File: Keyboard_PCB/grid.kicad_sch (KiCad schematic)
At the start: 140 parts, among them SW1 ESC, SW10 9, SW11 0, SW12 -, SW13 =, SW14 <-, SW15 DEL, SW16 TAB, SW17 Q, SW18 W, SW19 E, SW2 1, SW20 R, SW21 T, SW22 Y, SW23 U, SW24 I, SW25 O, SW26 P, SW27 [, SW28 ], SW29 \, SW3 2, SW30 HOME, SW31 CAPS, SW32 A, SW33 S, SW34 D, SW35 F, SW36 G, SW37 H, SW38 J, SW39 K, SW4 3, SW40 L, SW41 ;, SW42 ', SW43 ENTER, SW44 PG_U, SW45 SHIFT, SW46 Z, SW47 X, SW48 C, SW49 V, SW5 4, SW50 B, SW51 N, SW52 M, SW53 ,, SW54 ., SW55 /, SW56 SHIFT, SW57 UP, SW58 PG_D, SW59 CTRL, SW6 5, SW60 CODE, SW61 ALT, SW62 SPACE, SW63 ALT, SW64 CODE, SW65 CTRL, SW66 LEFT, SW67 DOWN, SW68 RIGHT, SW69 EC11E15244G1, SW7 6, SW8 7, SW9 8

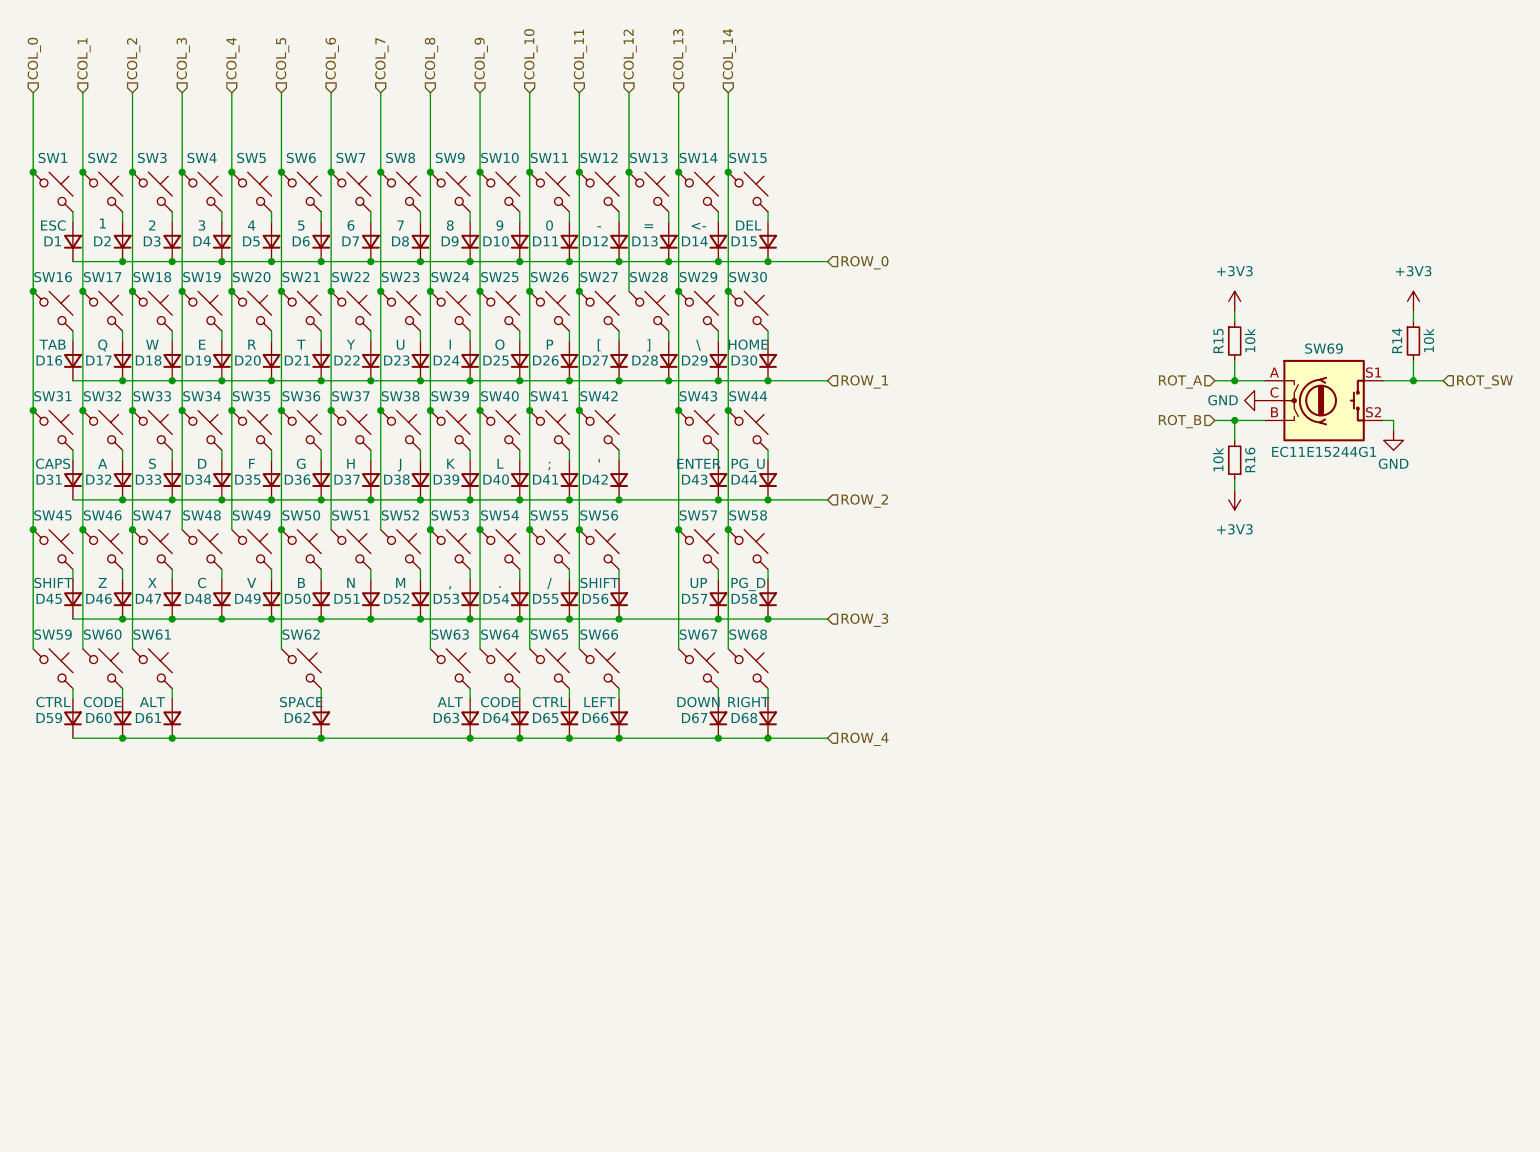
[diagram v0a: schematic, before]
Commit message: Fixed errors in BOM file
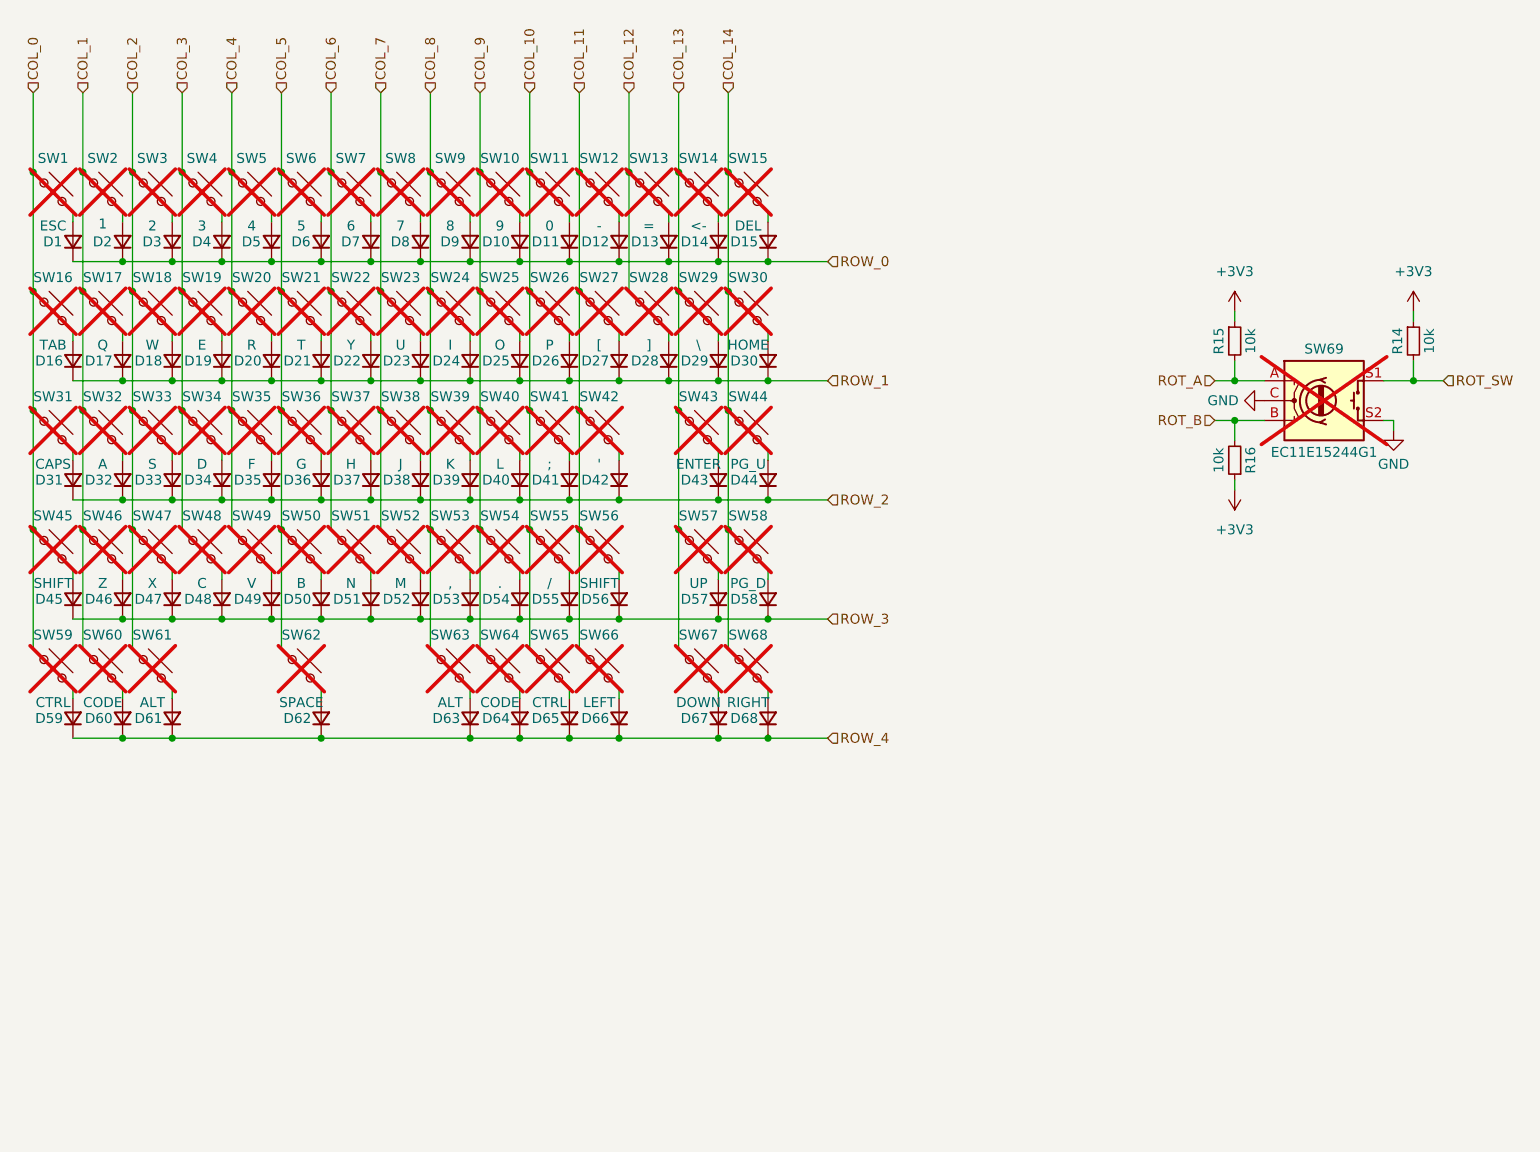
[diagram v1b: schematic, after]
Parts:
- SW1, SW10, SW11, SW12, SW13, SW14, SW15, SW16, SW17, SW18, SW19, SW2, SW20, SW21, SW22, SW23, SW24, SW25, SW26, SW27, SW28, SW29, SW3, SW30, SW31, SW32, SW33, SW34, SW35, SW36, SW37, SW38, SW39, SW4, SW40, SW41, SW42, SW43, SW44, SW45, SW46, SW47, SW48, SW49, SW5, SW50, SW51, SW52, SW53, SW54, SW55, SW56, SW57, SW58, SW59, SW6, SW60, SW61, SW62, SW63, SW64, SW65, SW66, SW67, SW68, SW69, SW7, SW8, SW9: now not fitted

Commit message: Found error in BOM
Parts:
- R14, R15, R16: LCSC C25879 -> C25744
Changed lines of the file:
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@@
 			)
 		)
-		(property "LCSC" "C25879"
+		(property "LCSC" "C25744"
 			(at 217.17 82.55 0)
 			(effects
@@
 			)
 		)
-		(property "LCSC" "C25879"
+		(property "LCSC" "C25744"
 			(at 240.03 82.55 0)
 			(effects
@@
 			)
 		)
-		(property "LCSC" "C25879"
+		(property "LCSC" "C25744"
 			(at 217.17 97.79 0)
 			(effects

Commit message: LCD-overhead test
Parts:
- added R14, R16, R6: 10k, Resistor_SMD:R_0402_1005Metric, symbol Device:R_Small
- added SW70: EC11E15244G1, Rotary_Encoder:RotaryEncoder_Alps_EC11E-Switch_Vertical_H20mm, symbol Device:RotaryEncoder_Switch
- renumbered R16 to R15, R15 to R4, R14 to R5
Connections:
- net +3V3: now also R14.1, R16.1, R6.1
- net GND: now also SW70.C, SW70.S2
- net ROT_A: now also R6.2, SW70.A
- net ROT_B: now also R16.2, SW70.B
- net ROT_SW: now also R14.2, SW70.S1
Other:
- moved on the sheet: R15, R4, R5, SW69

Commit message: USB placement
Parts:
- SW69: footprint Rotary_Encoder:RotaryEncoder_Alps_EC11E-Switch_Vertical_H20mm -> Marijn_KiCad:EC11E-Switch-No_MP
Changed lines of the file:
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@@
 			)
 		)
-		(property "Footprint" "Rotary_Encoder:RotaryEncoder_Alps_EC11E-Switch_Vertical_H20mm"
+		(property "Footprint" "Marijn_KiCad:EC11E-Switch-No_MP"
 			(at 81.28 162.306 0)
 			(effects

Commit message: Layout progress
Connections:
- net ROT_A renamed ROT0_A
- net ROT0_A: no longer R6.2, SW70.A
- net ROT_B renamed ROT0_B
- net ROT0_B: no longer R16.2, SW70.B
- net ROT_SW renamed ROT0_SW
- net ROT0_SW: no longer R14.2, SW70.S1
- new net ROT1_A: R6.2, SW70.A
- new net ROT1_B: R16.2, SW70.B
- new net ROT1_SW: R14.2, SW70.S1
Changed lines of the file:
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@@
 		)
 	)
-	(hierarchical_label "ROT_SW"
+	(hierarchical_label "ROT0_SW"
 		(shape input)
 		(at 100.33 163.83 0)
@@
 		)
 	)
-	(hierarchical_label "ROT_B"
+	(hierarchical_label "ROT0_B"
 		(shape input)
 		(at 71.12 168.91 180)
@@
 		)
 	)
-	(hierarchical_label "ROT_B"
+	(hierarchical_label "ROT1_B"
 		(shape input)
 		(at 124.46 168.91 180)
@@
 		)
 	)
-	(hierarchical_label "ROT_A"
+	(hierarchical_label "ROT0_A"
 		(shape input)
 		(at 71.12 163.83 180)
@@
 		)
 	)
-	(hierarchical_label "ROT_A"
+	(hierarchical_label "ROT1_A"
 		(shape input)
 		(at 124.46 163.83 180)
@@
 		)
 	)
-	(hierarchical_label "ROT_SW"
+	(hierarchical_label "ROT1_SW"
 		(shape input)
 		(at 153.67 163.83 0)

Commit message: Finished Layout V1
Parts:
- R14, R15, R16, R4, R5, R6: footprint Resistor_SMD:R_0402_1005Metric -> Resistor_SMD:R_0603_1608Metric
- SW1, SW10, SW11, SW12, SW13, SW14, SW15, SW16, SW17, SW18, SW19, SW2, SW20, SW21, SW22, SW23, SW24, SW25, SW26, SW27, SW28, SW29, SW3, SW30, SW31, SW32, SW33, SW34, SW35, SW36, SW37, SW38, SW39, SW4, SW40, SW41, SW42, SW43, SW44, SW45, SW46, SW47, SW48, SW49, SW5, SW50, SW51, SW52, SW53, SW54, SW55, SW56, SW57, SW58, SW59, SW6, SW60, SW61, SW62, SW63, SW64, SW65, SW66, SW67, SW68, SW69, SW7, SW70, SW8, SW9: now fitted

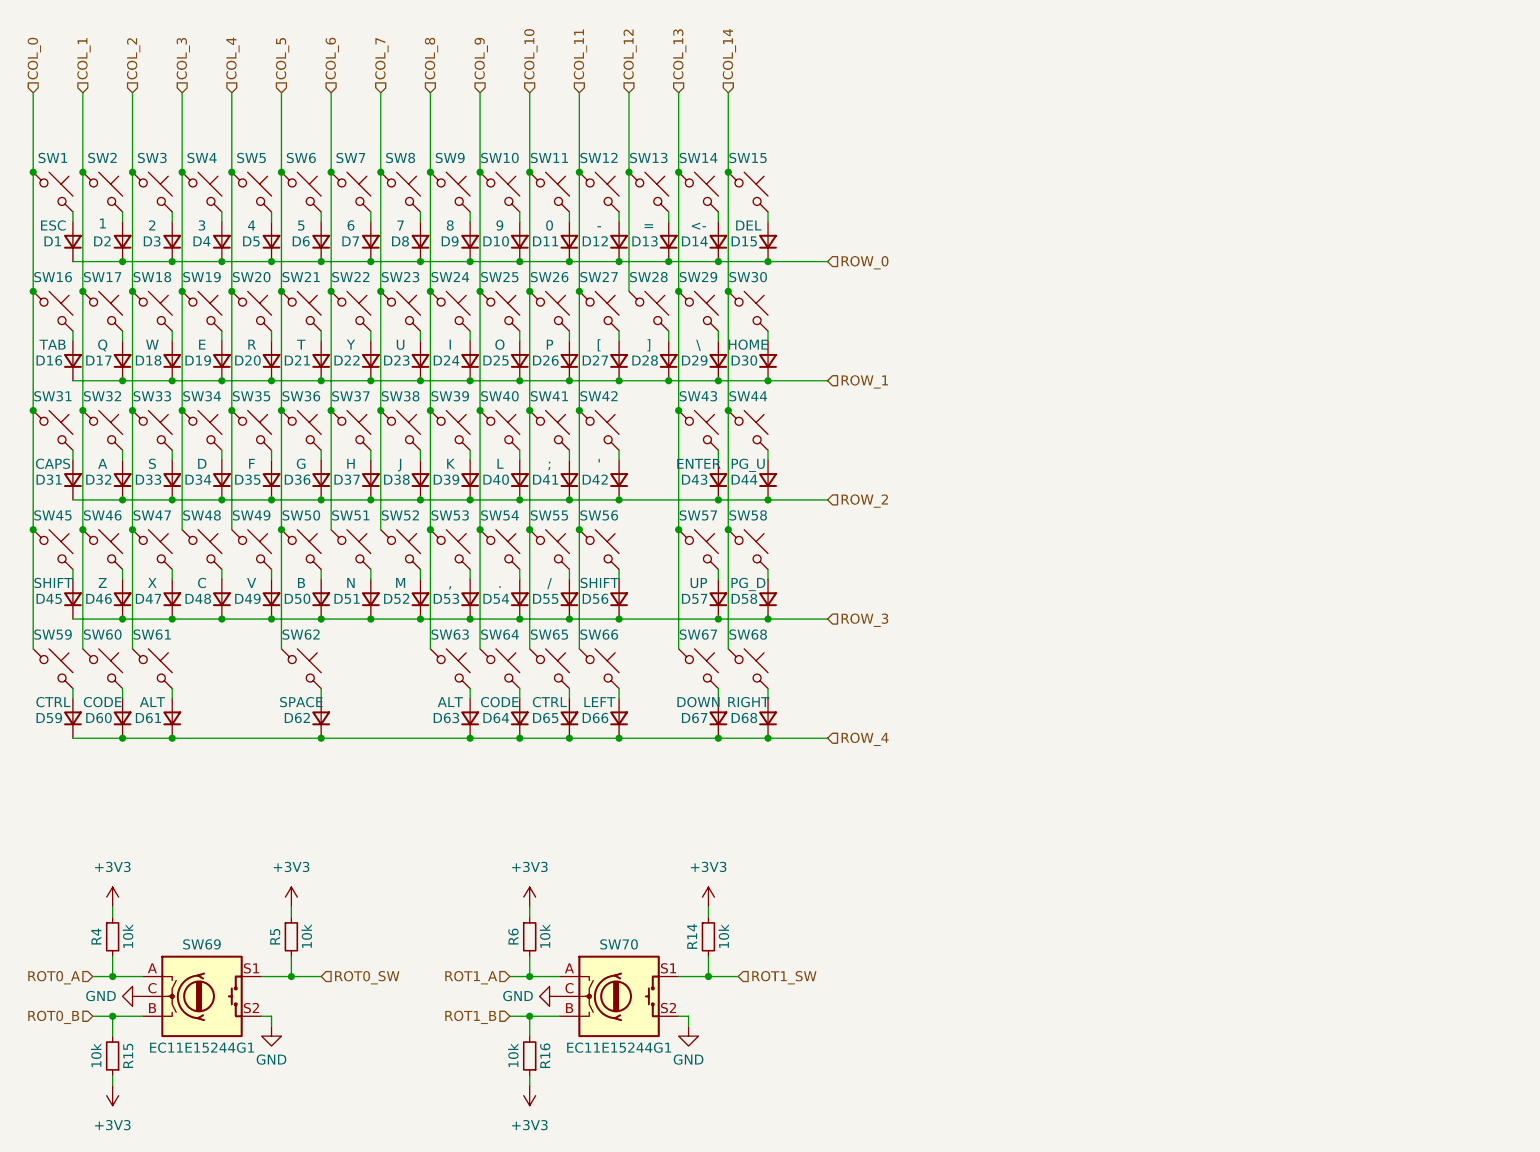
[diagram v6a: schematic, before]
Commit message: Keyboard V2 outline
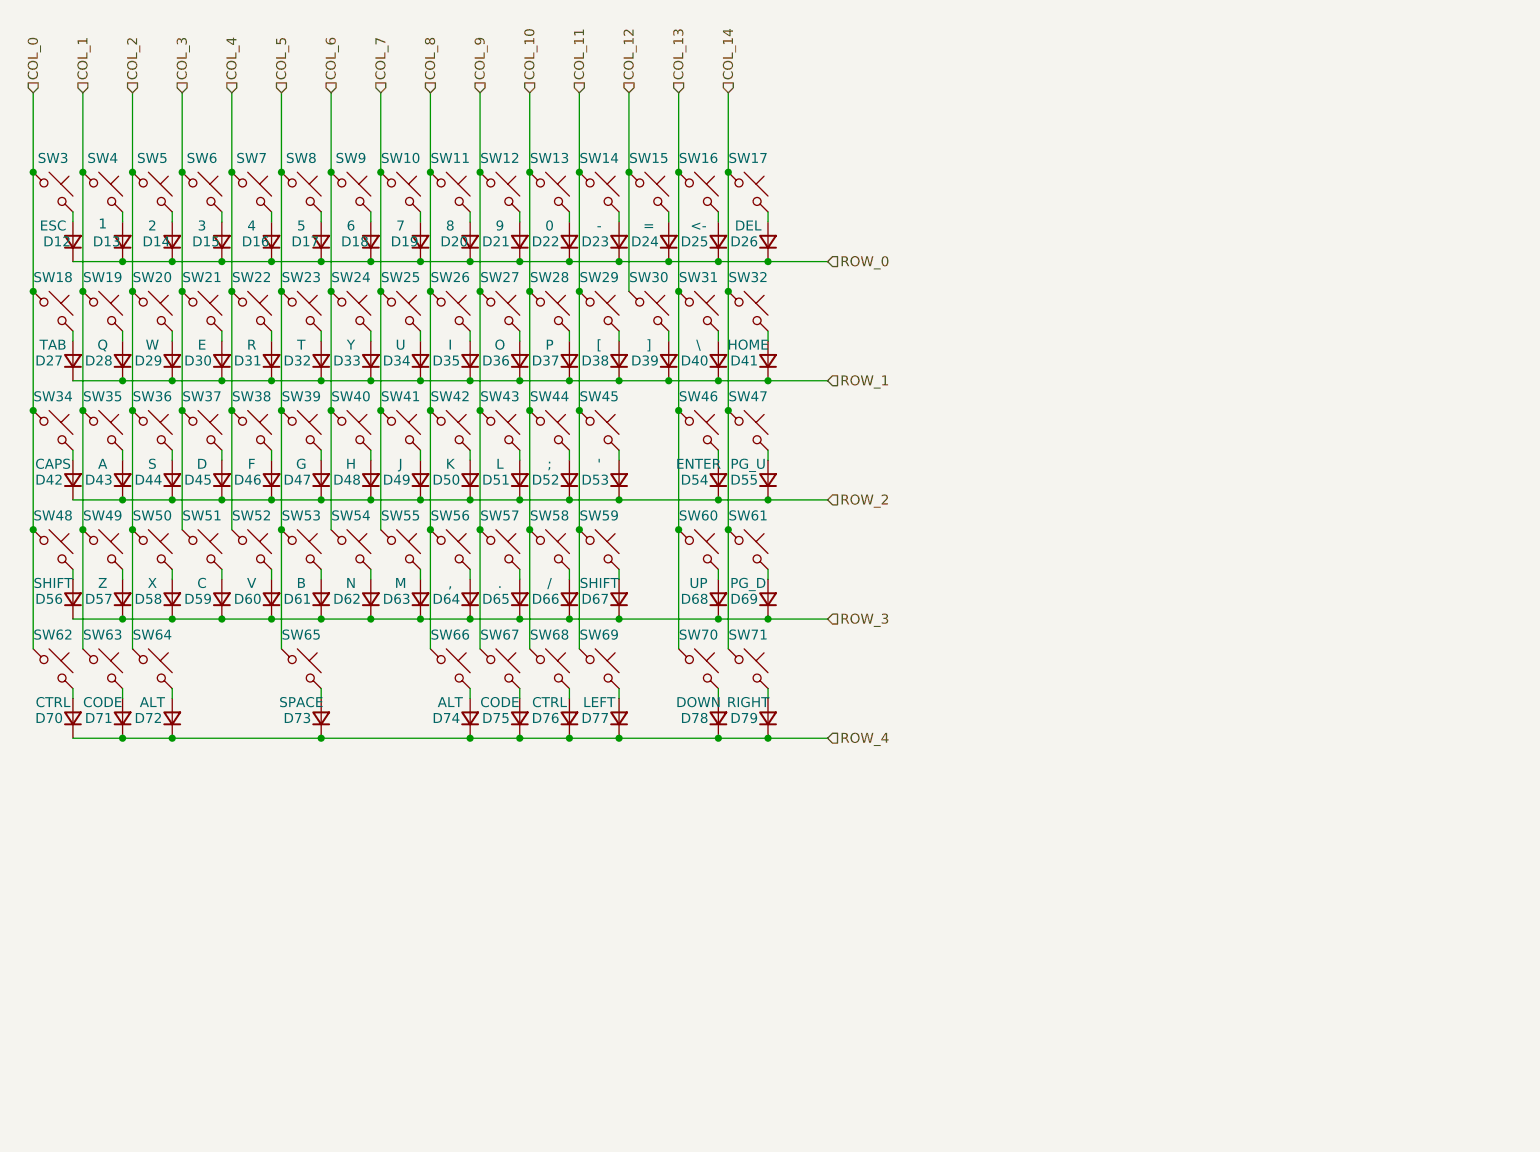
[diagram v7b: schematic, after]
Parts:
- removed R14, R15, R16, R4, R5, R6: 10k, Resistor_SMD:R_0603_1608Metric, symbol Device:R_Small
- removed SW69: EC11E15244G1, Marijn_KiCad:EC11E-Switch-No_MP, symbol Device:RotaryEncoder_Switch
- removed SW70: EC11E15244G1, Rotary_Encoder:RotaryEncoder_Alps_EC11E-Switch_Vertical_H20mm, symbol Device:RotaryEncoder_Switch
- renumbered D1 to D12, D2 to D13, D3 to D14, D4 to D15, D5 to D16, D6 to D17, D7 to D18, D8 to D19, D9 to D20, D10 to D21, D11 to D22, D12 to D23, D13 to D24, D14 to D25, D15 to D26, D16 to D27, D17 to D28, D18 to D29, D19 to D30, D20 to D31, D21 to D32, D22 to D33, D23 to D34, D24 to D35, D25 to D36, D26 to D37, D27 to D38, D28 to D39, D29 to D40, D30 to D41, D31 to D42, D32 to D43, D33 to D44, D34 to D45, D35 to D46, D36 to D47, D37 to D48, D38 to D49, D39 to D50, D40 to D51, D41 to D52, D42 to D53, D43 to D54, D44 to D55, D45 to D56, D46 to D57, D47 to D58, D48 to D59, D49 to D60, D50 to D61, D51 to D62, D52 to D63, D53 to D64, D54 to D65, D55 to D66, D56 to D67, D57 to D68, D58 to D69, D59 to D70, D60 to D71, D61 to D72, D62 to D73, D63 to D74, D64 to D75, D65 to D76, D66 to D77, D67 to D78, D68 to D79, SW8 to SW10, SW9 to SW11, SW10 to SW12, SW11 to SW13, SW12 to SW14, SW13 to SW15, SW14 to SW16, SW15 to SW17, SW16 to SW18, SW17 to SW19, SW18 to SW20, SW19 to SW21, SW20 to SW22, SW21 to SW23, SW22 to SW24, SW23 to SW25, SW24 to SW26, SW25 to SW27, SW26 to SW28, SW27 to SW29, SW1 to SW3, SW28 to SW30, SW29 to SW31, SW30 to SW32, SW31 to SW34, SW32 to SW35, SW33 to SW36, SW34 to SW37, SW35 to SW38, SW36 to SW39, SW2 to SW4, SW37 to SW40, SW38 to SW41, SW39 to SW42, SW40 to SW43, SW41 to SW44, SW42 to SW45, SW43 to SW46, SW44 to SW47, SW45 to SW48, SW46 to SW49, SW3 to SW5, SW47 to SW50, SW48 to SW51, SW49 to SW52, SW50 to SW53, SW51 to SW54, SW52 to SW55, SW53 to SW56, SW54 to SW57, SW55 to SW58, SW56 to SW59, SW4 to SW6, SW57 to SW60, SW58 to SW61, SW59 to SW62, SW60 to SW63, SW61 to SW64, SW62 to SW65, SW63 to SW66, SW64 to SW67, SW65 to SW68, SW66 to SW69, SW5 to SW7, SW67 to SW70, SW68 to SW71, SW6 to SW8, SW7 to SW9
